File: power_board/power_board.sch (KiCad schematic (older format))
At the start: 67 parts, among them J1 PROG, J10 M4, J11 5V_1, J12 M5, J13 M6, J14 M7, J15 FAN, J16 Screw_Terminal_01x02, J17 MB_interface, J18 Conn_01x02_Female, J19 12V_1, J2 M1, J20 12V_2, J21 12V_3, J22 12V_4, J23 48V_1, J24 48V_2, J25 48V_3, J26 48V_4, J3 M2, J4 Conn_01x02_Female, J5 Conn_01x02_Female, J6 Conn_01x01_Male, J7 Conn_01x01_Male, J8 Screw_Terminal_01x02, J9 M3, Q1 2N3906, SW1 SW_Push, U1 ACS758xCB-050B-PFF, U2 ACS758xCB-050B-PFF, U3 MCP2515-EST, U4 MAX31855KASA, U5 MCP2551-I-SN, U6 BTS50085-1TMA, U7 ATmega328P-AU, U8 BTS50085-1TMA, U9 LM2596S-5, Y1 20Mhz, Y2 16Mhz

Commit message: working on microcontroller routing
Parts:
- D2, D3: footprint Diode_SMD:D_0603_1608Metric -> Diode_SMD:D_SMB
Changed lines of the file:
@@
 F 0 "D2" H 7000 2000 50  0000 C CNN
 F 1 "1N5824" H 7000 2200 50  0000 C CNN
-F 2 "Diode_SMD:D_0603_1608Metric" H 7000 2100 50  0001 C CNN
+F 2 "Diode_SMD:D_SMB" H 7000 2100 50  0001 C CNN
 F 3 "~" H 7000 2100 50  0001 C CNN
 	1    7000 2100
@@
 F 0 "D3" H 7800 1684 50  0000 C CNN
 F 1 "--" H 7800 1775 50  0000 C CNN
-F 2 "Diode_SMD:D_0603_1608Metric" H 7800 1900 50  0001 C CNN
+F 2 "Diode_SMD:D_SMB" H 7800 1900 50  0001 C CNN
 F 3 "~" H 7800 1900 50  0001 C CNN
 	1    7800 1900

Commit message: finishing touches
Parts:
- Y2: footprint Crystal:Resonator_SMD-3Pin_7.2x3.0mm -> CSTCE16M0V53-R0:OSC_CSTCE16M0V53-R0
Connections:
- wire segments 284 -> 288
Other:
- note added: "D4"
- moved on the sheet: C1, C2
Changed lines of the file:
@@
 L Device:CP C1
 U 1 1 5BA44640
-P 2600 4650
-F 0 "C1" H 2500 4450 50  0000 L CNN
-F 1 "300uF" H 2500 4350 50  0000 L CNN
-F 2 "Capacitor_THT:CP_Radial_D10.0mm_P7.50mm" H 2638 4500 50  0001 C CNN
-F 3 "~" H 2600 4650 50  0001 C CNN
-	1    2600 4650
+P 1350 3850
+F 0 "C1" H 1150 3950 50  0000 L CNN
+F 1 "300uF" H 1100 3750 50  0000 L CNN
+F 2 "Capacitor_THT:CP_Radial_D10.0mm_P7.50mm" H 1388 3700 50  0001 C CNN
+F 3 "~" H 1350 3850 50  0001 C CNN
+	1    1350 3850
 	1    0    0    -1
 $EndComp
@@
 L Device:CP C2
 U 1 1 5BA446DC
-P 2600 5900
-F 0 "C2" H 2500 5700 50  0000 L CNN
-F 1 "300uF" H 2500 5600 50  0000 L CNN
-F 2 "Capacitor_THT:CP_Radial_D10.0mm_P7.50mm" H 2638 5750 50  0001 C CNN
-F 3 "~" H 2600 5900 50  0001 C CNN
-	1    2600 5900
+P 1650 3850
+F 0 "C2" H 1700 3950 50  0000 L CNN
+F 1 "300uF" H 1100 3750 50  0000 L CNN
+F 2 "Capacitor_THT:CP_Radial_D10.0mm_P7.50mm" H 1688 3700 50  0001 C CNN
+F 3 "~" H 1650 3850 50  0001 C CNN
+	1    1650 3850
 	1    0    0    -1
 $EndComp
@@
 	12800 7800 12800 7700
 $Comp
-L Device:Resonator Y2
-U 1 1 5BA74C01
-P 15050 5650
-F 0 "Y2" V 15350 5500 50  0000 L CNN
-F 1 "16Mhz" V 15250 5350 50  0000 L CNN
-F 2 "Crystal:Resonator_SMD-3Pin_7.2x3.0mm" H 15025 5650 50  0001 C CNN
-F 3 "~" H 15025 5650 50  0001 C CNN
-	1    15050 5650
-	0    -1   -1   0
-$EndComp
-$Comp
 L power:GNDREF #PWR0125
 U 1 1 5BA7A004
@@
 	1    0    0    -1
 $EndComp
+Text GLabel 14650 6000 2    50   Input ~ 0
+12V_SENSE
 Text GLabel 14650 5900 2    50   Input ~ 0
-12V_SENSE
-Text GLabel 14650 6000 2    50   Input ~ 0
 12VA_SENSE
 Wire Wire Line
@@
 Text GLabel 14800 5350 2    50   Input ~ 0
 SCK
-Text GLabel 14600 7300 2    50   Input ~ 0
+Text GLabel 14600 7100 2    50   Input ~ 0
 TC_CS
 Wire Wire Line
-	14500 7300 14600 7300
-Wire Wire Line
 	14800 5600 14800 5500
 Wire Wire Line
@@
 	14800 5700 14800 5800
 Wire Wire Line
-	14800 5800 15050 5800
-Wire Wire Line
 	14500 5700 14800 5700
-Wire Wire Line
-	15250 5650 15400 5650
 $Comp
 L Device:R_US R8
@@
 Wire Wire Line
 	8200 8550 8250 8550
-Text GLabel 14600 6900 2    50   Input ~ 0
+Text GLabel 14600 7000 2    50   Input ~ 0
 CAN_INT
 Wire Wire Line
@@
 	1    0    0    -1
 $EndComp
+Text GLabel 9250 5550 0    50   Input ~ 0
+TX
 Text GLabel 9250 5450 0    50   Input ~ 0
-TX
-Text GLabel 9250 5550 0    50   Input ~ 0
 RX
 Wire Wire Line
@@
 L power:GNDREF #PWR0101
 U 1 1 5BABAFE5
-P 2850 4950
-F 0 "#PWR0101" H 2850 4700 50  0001 C CNN
-F 1 "GNDREF" H 2855 4777 50  0000 C CNN
-F 2 "" H 2850 4950 50  0001 C CNN
-F 3 "" H 2850 4950 50  0001 C CNN
-	1    2850 4950
+P 1500 4000
+F 0 "#PWR0101" H 1500 3750 50  0001 C CNN
+F 1 "GNDREF" H 1505 3827 50  0000 C CNN
+F 2 "" H 1500 4000 50  0001 C CNN
+F 3 "" H 1500 4000 50  0001 C CNN
+	1    1500 4000
 	1    0    0    -1
 $EndComp
@@
 Wire Wire Line
 	8200 8650 8250 8650
-Text GLabel 14600 7000 2    50   Input ~ 0
+Text GLabel 14600 6900 2    50   Input ~ 0
 RX_INT
 Wire Wire Line
@@
 Text GLabel 14650 6100 2    50   Input ~ 0
 RX1BF
-Text GLabel 14650 6200 2    50   Input ~ 0
+Text GLabel 14650 6400 2    50   Input ~ 0
 TX0RTS
 Text GLabel 14650 6300 2    50   Input ~ 0
 TX1RTS
-Text GLabel 14650 6400 2    50   Input ~ 0
+Text GLabel 14650 6200 2    50   Input ~ 0
 TX2RTS
 Wire Wire Line
@@
 	2850 4650 2850 4800
 Connection ~ 2850 4800
-Connection ~ 2600 4500
-Wire Wire Line
-	2600 4500 2450 4500
-Wire Wire Line
-	2600 4500 2900 4500
-Wire Wire Line
-	2600 4800 2850 4800
 Connection ~ 2600 5750
 Wire Wire Line
 	2600 5750 2450 5750
-Wire Wire Line
-	2850 6050 2600 6050
 Wire Wire Line
 	2600 5750 2900 5750
@@
 NoConn ~ 9350 8300
 NoConn ~ 14500 7400
-NoConn ~ 14500 7100
+NoConn ~ 14500 7300
 NoConn ~ 14500 5000
 NoConn ~ 14500 5100
@@
 L power:+5V #PWR0159
 U 1 1 5BC39A5C
-P 11350 5400
-F 0 "#PWR0159" H 11350 5250 50  0001 C CNN
-F 1 "+5V" H 11365 5573 50  0000 C CNN
-F 2 "" H 11350 5400 50  0001 C CNN
-F 3 "" H 11350 5400 50  0001 C CNN
-	1    11350 5400
+P 11200 5950
+F 0 "#PWR0159" H 11200 5800 50  0001 C CNN
+F 1 "+5V" H 11215 6123 50  0000 C CNN
+F 2 "" H 11200 5950 50  0001 C CNN
+F 3 "" H 11200 5950 50  0001 C CNN
+	1    11200 5950
 	1    0    0    -1
 $EndComp
@@
 L power:GNDREF #PWR0160
 U 1 1 5BC39AEB
-P 11350 5800
-F 0 "#PWR0160" H 11350 5550 50  0001 C CNN
-F 1 "GNDREF" H 11355 5627 50  0000 C CNN
-F 2 "" H 11350 5800 50  0001 C CNN
-F 3 "" H 11350 5800 50  0001 C CNN
-	1    11350 5800
-	1    0    0    -1
-$EndComp
-Wire Wire Line
-	11350 5450 11350 5400
-Wire Wire Line
-	11350 5800 11350 5750
+P 11750 5300
+F 0 "#PWR0160" H 11750 5050 50  0001 C CNN
+F 1 "GNDREF" H 11755 5127 50  0000 C CNN
+F 2 "" H 11750 5300 50  0001 C CNN
+F 3 "" H 11750 5300 50  0001 C CNN
+	1    11750 5300
+	1    0    0    -1
+$EndComp
 Text GLabel 11250 5550 0    50   Input ~ 0
 CANH
@@
 Wire Wire Line
 	1400 8400 1400 8650
+Wire Wire Line
+	14800 5800 15050 5800
+Wire Wire Line
+	15250 5650 15400 5650
+$Comp
+L Device:Resonator Y2
+U 1 1 5BA74C01
+P 15050 5650
+F 0 "Y2" V 15350 5500 50  0000 L CNN
+F 1 "16Mhz" V 15250 5350 50  0000 L CNN
+F 2 "CSTCE16M0V53-R0:OSC_CSTCE16M0V53-R0" H 15025 5650 50  0001 C CNN
+F 3 "~" H 15025 5650 50  0001 C CNN
+	1    15050 5650
+	0    -1   -1   0
+$EndComp
+Wire Wire Line
+	14500 7100 14600 7100
+Text Notes 14200 7150 2    50   ~ 0
+D4
+Wire Wire Line
+	11200 5950 11350 5950
+Wire Wire Line
+	11350 5950 11350 5750
+Wire Wire Line
+	11350 5450 11350 5300
+Wire Wire Line
+	11350 5300 11750 5300
+Wire Wire Line
+	2450 4500 2900 4500
+Wire Wire Line
+	1650 4000 1500 4000
+Wire Wire Line
+	1350 4000 1500 4000
+Connection ~ 1500 4000
+Wire Wire Line
+	1650 3700 1500 3700
+$Comp
+L power:+48V #PWR0161
+U 1 1 5BD4F164
+P 1500 3650
+F 0 "#PWR0161" H 1500 3500 50  0001 C CNN
+F 1 "+48V" H 1515 3823 50  0000 C CNN
+F 2 "" H 1500 3650 50  0001 C CNN
+F 3 "" H 1500 3650 50  0001 C CNN
+	1    1500 3650
+	1    0    0    -1
+$EndComp
+Wire Wire Line
+	1500 3650 1500 3700
+Connection ~ 1500 3700
+Wire Wire Line
+	1500 3700 1350 3700
+$Comp
+L power:GNDREF #PWR?
+U 1 1 5BD67F28
+P 2850 4950
+F 0 "#PWR?" H 2850 4700 50  0001 C CNN
+F 1 "GNDREF" H 2855 4777 50  0000 C CNN
+F 2 "" H 2850 4950 50  0001 C CNN
+F 3 "" H 2850 4950 50  0001 C CNN
+	1    2850 4950
+	1    0    0    -1
+$EndComp
 $EndSCHEMATC

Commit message: Finished final Draft of design
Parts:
- Y1: footprint Crystal:Resonator_SMD-3Pin_7.2x3.0mm -> Crystal:Crystal_SMD_0603-2Pin_6.0x3.5mm
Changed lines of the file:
@@
 U 1 1 5BB39D19
 P 6600 8800
-F 0 "Y1" V 6300 8850 50  0000 L CNN
-F 1 "20Mhz" V 6400 8850 50  0000 L CNN
-F 2 "Crystal:Resonator_SMD-3Pin_7.2x3.0mm" H 6600 8800 50  0001 C CNN
+F 0 "Y1" V 6700 8600 50  0000 L CNN
+F 1 "20Mhz" V 6600 8450 50  0000 L CNN
+F 2 "Crystal:Crystal_SMD_0603-2Pin_6.0x3.5mm" H 6600 8800 50  0001 C CNN
 F 3 "~" H 6600 8800 50  0001 C CNN
 	1    6600 8800
-	0    1    1    0
+	0    -1   -1   0
 $EndComp
 $Comp
@@
 	1500 3700 1350 3700
 $Comp
-L power:GNDREF #PWR?
+L power:GNDREF #PWR0162
 U 1 1 5BD67F28
 P 2850 4950
-F 0 "#PWR?" H 2850 4700 50  0001 C CNN
+F 0 "#PWR0162" H 2850 4700 50  0001 C CNN
 F 1 "GNDREF" H 2855 4777 50  0000 C CNN
 F 2 "" H 2850 4950 50  0001 C CNN

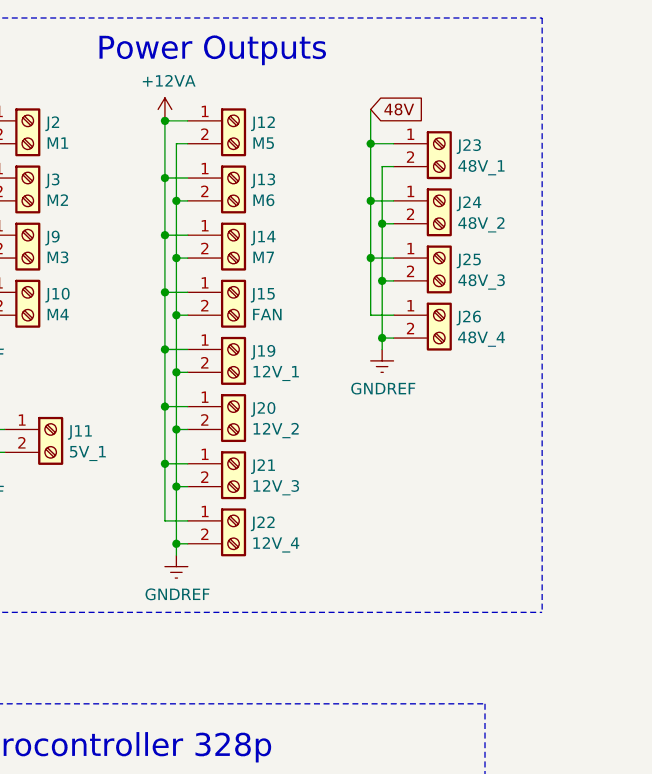
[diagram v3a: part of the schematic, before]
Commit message: Added fuses
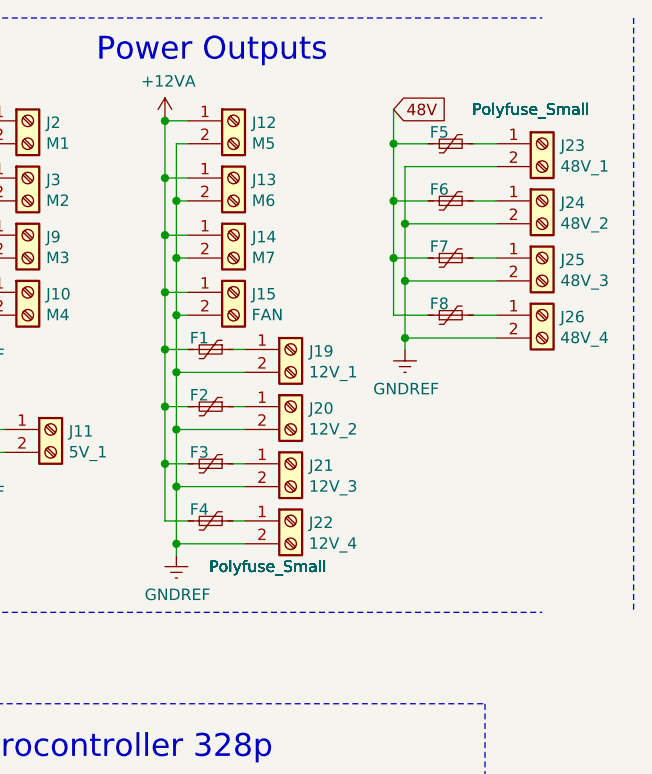
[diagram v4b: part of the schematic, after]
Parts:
- added F1, F2, F3, F4, F5, F6, F7, F8: Polyfuse_Small, Fuse:Fuse_1206_3216Metric, symbol Device:Polyfuse_Small
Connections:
- wire segments 288 -> 296
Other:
- moved on the sheet: J19, J20, J21, J22, J23, J24, J25, J26

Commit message: post-board review edits
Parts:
- removed D3: --, Diode_SMD:D_SMB, symbol Device:D_Schottky
- added C6: 0.1uF, Capacitor_SMD:C_0603_1608Metric, symbol Device:C
- added J27: Screw_Terminal_01x02, Connector_PinHeader_2.54mm:PinHeader_1x02_P2.54mm_Vertical, symbol Connector:Screw_Terminal_01x02
- added R10: 10k, Resistor_SMD:R_0603_1608Metric, symbol Device:R_US
- added U10: MAX31855KASA, Package_SO:SOIC-8_3.9x4.9mm_P1.27mm, symbol Sensor_Temperature:MAX31855KASA
- C14, C15: symbol Device:C -> Device:CP
- J8: footprint TerminalBlock:TerminalBlock_bornier-2_P5.08mm -> Connector_PinHeader_2.54mm:PinHeader_1x02_P2.54mm_Vertical
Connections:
- net labels added: TC1_CS, TC2_CS
- net labels removed: TC_CS
- wire segments 296 -> 312
- no-connect marks 14 -> 13
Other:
- moved on the sheet: C7, C8, C9, J8, R8, U1, U2, U4

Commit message: finished re-routing for v_prog diode
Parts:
- added D3: D_x2_KCom_AAK, Package_TO_SOT_SMD:SOT-23, symbol Device:D_x2_KCom_AAK
- REG1, REG2: symbol Delta-Q54SG_600W:StepDownConverter -> power_board-rescue:StepDownConverter-Delta-Q54SG_600W
- U7: symbol MCU_Microchip_ATmega:ATmega328P-AU -> power_board-rescue:ATmega328P-AU-MCU_Microchip_ATmega
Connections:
- net labels added: VPP, V_MCU
- wire segments 312 -> 318
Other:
- moved on the sheet: C13, R14, SW1, U7, Y2

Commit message: Added 3d models, finished design
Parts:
- removed U5: MCP2551-I-SN, Package_SO:SOIC-8_3.9x4.9mm_P1.27mm, symbol Interface_CAN_LIN:MCP2551-I-SN
- added U5: ATA6560,1, Package_SO:SOIC-8_3.9x4.9mm_P1.27mm, symbol URT_cache:ATA6560,1
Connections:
- net +5V: now also R9.2, U5.3 (VCC)
- net CANH: now also U5.7 (CANH)
- net CANL: now also U5.6 (CANL)
- net CAN_RX: now also U5.4 (RXD)
- net CAN_TX: now also U5.1 (TXD)
- net GNDREF: now also U5.2 (GND), U5.8 (STBY); no longer R9.1
- new net: R9.1, U5.5 (NSIL/VIO)
- no-connect marks 13 -> 12
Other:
- moved on the sheet: C10, J16
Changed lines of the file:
@@
-$EndComp
-$Comp
-L Interface_CAN_LIN:MCP2551-I-SN U5
-U 1 1 5BA69EE0
-P 9850 8200
-F 0 "U5" H 9950 8800 50  0000 C CNN
-F 1 "MCP2551-I-SN" H 10200 8700 50  0000 C CNN
-F 2 "Package_SO:SOIC-8_3.9x4.9mm_P1.27mm" H 9850 7700 50  0001 C CIN
-F 3 "http://ww1.microchip.com/downloads/en/devicedoc/21667d.pdf" H 9850 8200 50  0001 C CNN
-	1    9850 8200
-	1    0    0    -1
-$EndComp
-Text GLabel 9300 8000 0    50   Input ~ 0
-CAN_TX
-Text GLabel 9300 8100 0    50   Input ~ 0
-CAN_RX
-$Comp
-L power:+5V #PWR0143
-U 1 1 5BA77637
-P 9850 7550
-F 0 "#PWR0143" H 9850 7400 50  0001 C CNN
-F 1 "+5V" H 9865 7723 50  0000 C CNN
-F 2 "" H 9850 7550 50  0001 C CNN
-F 3 "" H 9850 7550 50  0001 C CNN
-	1    9850 7550
-	1    0    0    -1
-$EndComp
-$Comp
-L power:GNDREF #PWR0144
-U 1 1 5BA77D6B
-P 9850 8750
-F 0 "#PWR0144" H 9850 8500 50  0001 C CNN
-F 1 "GNDREF" H 9855 8577 50  0000 C CNN
-F 2 "" H 9850 8750 50  0001 C CNN
-F 3 "" H 9850 8750 50  0001 C CNN
-	1    9850 8750
-	1    0    0    -1
 $EndComp
 $Comp
 L Device:C C10
 U 1 1 5BA784CE
-P 9400 7550
-F 0 "C10" H 9515 7596 50  0000 L CNN
-F 1 "0.1uF" H 9515 7505 50  0000 L CNN
-F 2 "Capacitor_SMD:C_0603_1608Metric" H 9438 7400 50  0001 C CNN
-F 3 "~" H 9400 7550 50  0001 C CNN
-	1    9400 7550
-	0    1    1    0
-$EndComp
-$Comp
-L power:GNDREF #PWR0145
-U 1 1 5BA788D6
-P 9150 7650
-F 0 "#PWR0145" H 9150 7400 50  0001 C CNN
-F 1 "GNDREF" H 9155 7477 50  0000 C CNN
-F 2 "" H 9150 7650 50  0001 C CNN
-F 3 "" H 9150 7650 50  0001 C CNN
-	1    9150 7650
-	1    0    0    -1
-$EndComp
-Wire Wire Line
-	9850 7550 9850 7800
-Wire Wire Line
-	9550 7550 9850 7550
-Connection ~ 9850 7550
-Wire Wire Line
-	9250 7550 9150 7550
-Wire Wire Line
-	9150 7550 9150 7650
-Wire Wire Line
-	9300 8000 9350 8000
-Wire Wire Line
-	9300 8100 9350 8100
+P 9050 8600
+F 0 "C10" H 8800 8700 50  0000 L CNN
+F 1 "0.1uF" H 8750 8600 50  0000 L CNN
+F 2 "Capacitor_SMD:C_0603_1608Metric" H 9088 8450 50  0001 C CNN
+F 3 "~" H 9050 8600 50  0001 C CNN
+	1    9050 8600
+	1    0    0    -1
+$EndComp
 $Comp
 L power:+5V #PWR0146
@@
 Wire Wire Line
 	8200 8050 8250 8050
-$Comp
-L Device:R_US R9
-U 1 1 5BB7FA96
-P 9350 8600
-F 0 "R9" V 9555 8600 50  0000 C CNN
-F 1 "4.7k" V 9464 8600 50  0000 C CNN
-F 2 "Resistor_SMD:R_0603_1608Metric" V 9390 8590 50  0001 C CNN
-F 3 "~" H 9350 8600 50  0001 C CNN
-	1    9350 8600
-	-1   0    0    1
-$EndComp
-Wire Wire Line
-	9350 8400 9350 8450
-Wire Wire Line
-	9350 8750 9850 8750
-Wire Wire Line
-	9850 8600 9850 8750
-Connection ~ 9850 8750
-Text GLabel 10600 8100 2    50   Input ~ 0
-CANH
-Text GLabel 10600 8300 2    50   Input ~ 0
-CANL
 Text GLabel 8250 8550 2    50   Input ~ 0
 CAN_INT
@@
 Text Notes 2150 3500 0    100  ~ 0
 Power Regulation
-Wire Wire Line
-	10350 8300 10600 8300
-Wire Wire Line
-	10350 8100 10600 8100
 Text Notes 8800 6400 0    100  ~ 20
 VERIFY PIN ORDER!!!\n\n
@@
 NoConn ~ 3950 5900
 NoConn ~ 3950 4650
-NoConn ~ 9350 8300
 NoConn ~ 15050 7400
 NoConn ~ 15050 5000
@@
 L Connector:Screw_Terminal_01x02 J16
 U 1 1 5BEFA5C2
-P 10900 8850
-F 0 "J16" H 10900 8950 50  0000 C CNN
-F 1 "Screw_Terminal_01x02" H 10900 9400 50  0001 C CNN
-F 2 "TerminalBlock:TerminalBlock_bornier-2_P5.08mm" H 10900 8850 50  0001 C CNN
-F 3 "~" H 10900 8850 50  0001 C CNN
-	1    10900 8850
-	1    0    0    -1
-$EndComp
-Text GLabel 10500 8950 0    50   Input ~ 0
+P 13100 8800
+F 0 "J16" H 13100 8900 50  0000 C CNN
+F 1 "Screw_Terminal_01x02" H 13100 9350 50  0001 C CNN
+F 2 "TerminalBlock:TerminalBlock_bornier-2_P5.08mm" H 13100 8800 50  0001 C CNN
+F 3 "~" H 13100 8800 50  0001 C CNN
+	1    13100 8800
+	1    0    0    -1
+$EndComp
+Text GLabel 12700 8900 0    50   Input ~ 0
 CANH
-Text GLabel 10500 8850 0    50   Input ~ 0
+Text GLabel 12700 8800 0    50   Input ~ 0
 CANL
 $Comp
@@
 	13400 2950 13550 2950
 Wire Wire Line
-	10500 8850 10700 8850
-Wire Wire Line
-	10500 8950 10700 8950
+	12700 8800 12900 8800
+Wire Wire Line
+	12700 8900 12900 8900
 $Comp
 L power:+5V #PWR0159
@@
 Wire Wire Line
 	4550 8550 4550 8750
+$Comp
+L URT_cache:ATA6560,1 U5
+U 1 1 5BCC7310
+P 10150 8350
+F 0 "U5" H 10150 8915 50  0000 C CNN
+F 1 "ATA6560,1" H 10150 8824 50  0000 C CNN
+F 2 "Package_SO:SOIC-8_3.9x4.9mm_P1.27mm" H 10150 8850 50  0001 C CNN
+F 3 "" H 10150 8850 50  0001 C CNN
+	1    10150 8350
+	1    0    0    -1
+$EndComp
+$Comp
+L power:GNDREF #PWR0143
+U 1 1 5BD211AA
+P 9250 8900
+F 0 "#PWR0143" H 9250 8650 50  0001 C CNN
+F 1 "GNDREF" H 9255 8727 50  0000 C CNN
+F 2 "" H 9250 8900 50  0001 C CNN
+F 3 "" H 9250 8900 50  0001 C CNN
+	1    9250 8900
+	1    0    0    -1
+$EndComp
+Text GLabel 9650 8650 0    50   Input ~ 0
+CAN_RX
+Text GLabel 9650 8050 0    50   Input ~ 0
+CAN_TX
+$Comp
+L power:+5V #PWR0144
+U 1 1 5BD3FC89
+P 9200 7800
+F 0 "#PWR0144" H 9200 7650 50  0001 C CNN
+F 1 "+5V" H 9215 7973 50  0000 C CNN
+F 2 "" H 9200 7800 50  0001 C CNN
+F 3 "" H 9200 7800 50  0001 C CNN
+	1    9200 7800
+	1    0    0    -1
+$EndComp
+Wire Wire Line
+	9200 7800 9200 8450
+Text GLabel 10700 8450 2    50   Input ~ 0
+CANL
+Text GLabel 10700 8250 2    50   Input ~ 0
+CANH
+Wire Wire Line
+	10650 8250 10700 8250
+Wire Wire Line
+	10650 8450 10700 8450
+Wire Wire Line
+	9250 8250 9250 8750
+Wire Wire Line
+	9200 8450 9650 8450
+Wire Wire Line
+	9250 8250 9650 8250
+Wire Wire Line
+	9050 8450 9200 8450
+Connection ~ 9200 8450
+Wire Wire Line
+	9050 8750 9250 8750
+Connection ~ 9250 8750
+Wire Wire Line
+	9250 8750 9250 8900
+$Comp
+L Device:R_US R9
+U 1 1 5BE74A3F
+P 10850 8650
+F 0 "R9" V 10750 8750 50  0000 C CNN
+F 1 "4.7k" V 10750 8600 50  0000 C CNN
+F 2 "Resistor_SMD:R_0603_1608Metric" V 10890 8640 50  0001 C CNN
+F 3 "~" H 10850 8650 50  0001 C CNN
+	1    10850 8650
+	0    -1   -1   0
+$EndComp
+Wire Wire Line
+	10650 8650 10700 8650
+$Comp
+L power:+5V #PWR0145
+U 1 1 5BE94E58
+P 11050 8650
+F 0 "#PWR0145" H 11050 8500 50  0001 C CNN
+F 1 "+5V" H 11065 8823 50  0000 C CNN
+F 2 "" H 11050 8650 50  0001 C CNN
+F 3 "" H 11050 8650 50  0001 C CNN
+	1    11050 8650
+	1    0    0    -1
+$EndComp
+Wire Wire Line
+	11000 8650 11050 8650
+$Comp
+L power:GNDREF #PWR0152
+U 1 1 5BEB4CDE
+P 11150 8050
+F 0 "#PWR0152" H 11150 7800 50  0001 C CNN
+F 1 "GNDREF" H 11155 7877 50  0000 C CNN
+F 2 "" H 11150 8050 50  0001 C CNN
+F 3 "" H 11150 8050 50  0001 C CNN
+	1    11150 8050
+	1    0    0    -1
+$EndComp
+Wire Wire Line
+	10650 8050 11150 8050
 $EndSCHEMATC

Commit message: capacitor updates
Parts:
- added C11: 330uF, Capacitor_THT:CP_Radial_D10.0mm_P5.00mm, symbol Device:CP
- C1, C2: value 300uF -> 330uF; footprint Capacitor_THT:CP_Radial_D10.0mm_P7.50mm -> Capacitor_THT:CP_Radial_D10.0mm_P5.00mm
- R9: value 4.7k -> 10K
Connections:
- net +48V: now also C11.1
- net GNDREF: now also C11.2
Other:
- moved on the sheet: C1, C2
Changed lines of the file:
@@
 L Device:CP C1
 U 1 1 5BA44640
-P 1350 3850
-F 0 "C1" H 1150 3950 50  0000 L CNN
-F 1 "300uF" H 1100 3750 50  0000 L CNN
-F 2 "Capacitor_THT:CP_Radial_D10.0mm_P7.50mm" H 1388 3700 50  0001 C CNN
-F 3 "~" H 1350 3850 50  0001 C CNN
-	1    1350 3850
+P 3800 4050
+F 0 "C1" H 3600 4150 50  0000 L CNN
+F 1 "330uF" H 3550 3950 50  0000 L CNN
+F 2 "Capacitor_THT:CP_Radial_D10.0mm_P5.00mm" H 3838 3900 50  0001 C CNN
+F 3 "~" H 3800 4050 50  0001 C CNN
+	1    3800 4050
 	1    0    0    -1
 $EndComp
@@
 L Device:CP C2
 U 1 1 5BA446DC
-P 1650 3850
-F 0 "C2" H 1700 3950 50  0000 L CNN
-F 1 "300uF" H 1100 3750 50  0000 L CNN
-F 2 "Capacitor_THT:CP_Radial_D10.0mm_P7.50mm" H 1688 3700 50  0001 C CNN
-F 3 "~" H 1650 3850 50  0001 C CNN
-	1    1650 3850
+P 4100 4050
+F 0 "C2" H 4150 4150 50  0000 L CNN
+F 1 "330uF" H 3550 3950 50  0000 L CNN
+F 2 "Capacitor_THT:CP_Radial_D10.0mm_P5.00mm" H 4138 3900 50  0001 C CNN
+F 3 "~" H 4100 4050 50  0001 C CNN
+	1    4100 4050
 	1    0    0    -1
 $EndComp
@@
 L power:GNDREF #PWR0101
 U 1 1 5BABAFE5
-P 1500 4000
-F 0 "#PWR0101" H 1500 3750 50  0001 C CNN
-F 1 "GNDREF" H 1505 3827 50  0000 C CNN
-F 2 "" H 1500 4000 50  0001 C CNN
-F 3 "" H 1500 4000 50  0001 C CNN
-	1    1500 4000
+P 3950 4200
+F 0 "#PWR0101" H 3950 3950 50  0001 C CNN
+F 1 "GNDREF" H 3955 4027 50  0000 C CNN
+F 2 "" H 3950 4200 50  0001 C CNN
+F 3 "" H 3950 4200 50  0001 C CNN
+	1    3950 4200
 	1    0    0    -1
 $EndComp
@@
 	2450 4500 2900 4500
 Wire Wire Line
-	1650 4000 1500 4000
-Wire Wire Line
-	1350 4000 1500 4000
-Connection ~ 1500 4000
-Wire Wire Line
-	1650 3700 1500 3700
+	4100 4200 3950 4200
+Wire Wire Line
+	3800 4200 3950 4200
+Connection ~ 3950 4200
+Wire Wire Line
+	4100 3900 3950 3900
 $Comp
 L power:+48V #PWR0161
 U 1 1 5BD4F164
-P 1500 3650
-F 0 "#PWR0161" H 1500 3500 50  0001 C CNN
-F 1 "+48V" H 1515 3823 50  0000 C CNN
-F 2 "" H 1500 3650 50  0001 C CNN
-F 3 "" H 1500 3650 50  0001 C CNN
-	1    1500 3650
-	1    0    0    -1
-$EndComp
-Wire Wire Line
-	1500 3650 1500 3700
-Connection ~ 1500 3700
-Wire Wire Line
-	1500 3700 1350 3700
+P 3950 3850
+F 0 "#PWR0161" H 3950 3700 50  0001 C CNN
+F 1 "+48V" H 3965 4023 50  0000 C CNN
+F 2 "" H 3950 3850 50  0001 C CNN
+F 3 "" H 3950 3850 50  0001 C CNN
+	1    3950 3850
+	1    0    0    -1
+$EndComp
+Wire Wire Line
+	3950 3850 3950 3900
+Connection ~ 3950 3900
+Wire Wire Line
+	3950 3900 3800 3900
 $Comp
 L power:GNDREF #PWR0162
@@
 P 10850 8650
 F 0 "R9" V 10750 8750 50  0000 C CNN
-F 1 "4.7k" V 10750 8600 50  0000 C CNN
+F 1 "10K" V 10750 8600 50  0000 C CNN
 F 2 "Resistor_SMD:R_0603_1608Metric" V 10890 8640 50  0001 C CNN
 F 3 "~" H 10850 8650 50  0001 C CNN
@@
 Wire Wire Line
 	10650 8050 11150 8050
+$Comp
+L Device:CP C11
+U 1 1 5BCFC50C
+P 4400 4050
+F 0 "C11" H 4450 4150 50  0000 L CNN
+F 1 "330uF" H 3550 3950 50  0000 L CNN
+F 2 "Capacitor_THT:CP_Radial_D10.0mm_P5.00mm" H 4438 3900 50  0001 C CNN
+F 3 "~" H 4400 4050 50  0001 C CNN
+	1    4400 4050
+	1    0    0    -1
+$EndComp
+Wire Wire Line
+	4100 3900 4400 3900
+Connection ~ 4100 3900
+Wire Wire Line
+	4100 4200 4400 4200
+Connection ~ 4100 4200
 $EndSCHEMATC
